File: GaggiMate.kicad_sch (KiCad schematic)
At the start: 48 parts, among them J1 BTNS, J15 HX711 connector, J2 Heater SSR, J3 K-Type probe, J4 Conn_02x08_Odd_Even, J5 Analog sensors, J6 Pressure Sensor, J7 Debug Pins, J8 HV In, J9 Relays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

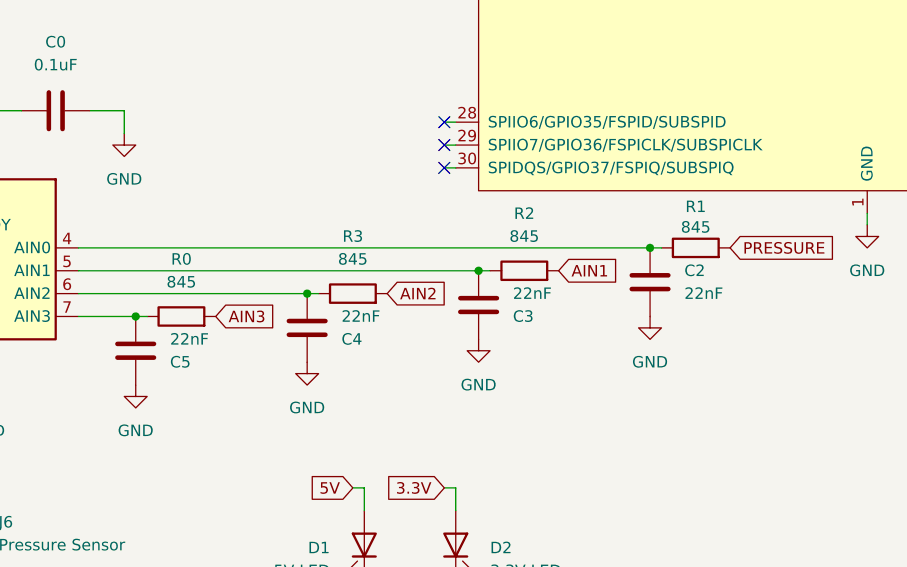
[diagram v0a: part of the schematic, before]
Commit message: update analog filters and started some HV traces
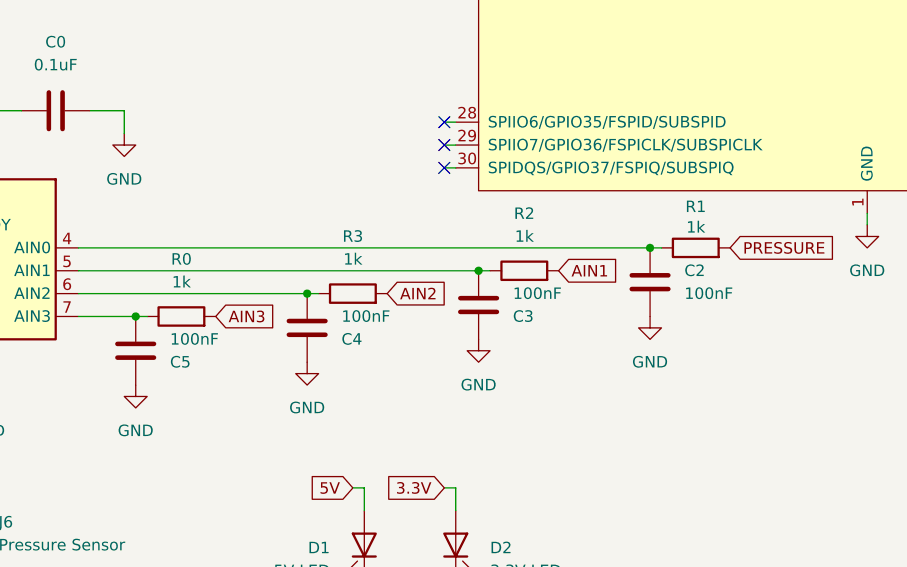
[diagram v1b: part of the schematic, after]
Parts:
- C2, C3, C4, C5: value 22nF -> 100nF
- R0, R1, R2, R3: value 845 -> 1k
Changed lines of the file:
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@@
 			)
 		)
-		(property "Value" "22nF"
+		(property "Value" "100nF"
 			(at 95.25 113.0301 0)
 			(effects
@@
 			)
 		)
-		(property "Value" "845"
+		(property "Value" "1k"
 			(at 77.47 109.22 90)
 			(effects
@@
 			)
 		)
-		(property "Value" "22nF"
+		(property "Value" "100nF"
 			(at 57.15 118.1101 0)
 			(effects
@@
 			)
 		)
-		(property "Value" "845"
+		(property "Value" "1k"
 			(at 115.57 105.664 90)
 			(effects
@@
 			)
 		)
-		(property "Value" "845"
+		(property "Value" "1k"
 			(at 96.52 106.68 90)
 			(effects
@@
 			)
 		)
-		(property "Value" "22nF"
+		(property "Value" "100nF"
 			(at 76.2 115.5701 0)
 			(effects
@@
 			)
 		)
-		(property "Value" "22nF"
+		(property "Value" "100nF"
 			(at 114.3 113.0299 0)
 			(effects
@@
 			)
 		)
-		(property "Value" "845"
+		(property "Value" "1k"
 			(at 58.42 111.76 90)
 			(effects

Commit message: more routing and and programming buttons
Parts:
- removed R4: 10k, Resistor_SMD:R_0603_1608Metric, symbol Device:R
- added C13, C14: 0.1uF, Capacitor_SMD:C_0603_1608Metric, symbol Device:C
- added C15: 10uF, Capacitor_SMD:C_0603_1608Metric, symbol Device:C
- added J16: UART, Connector_JST:JST_PH_B4B-PH-K_1x04_P2.00mm_Vertical, symbol Connector_Generic:Conn_01x04
- added SW1, SW2: SW_Push, Button_Switch_SMD:SW_SPST_TL3342, symbol Switch:SW_Push
- P0: footprint Connector_USB:USB_C_Receptacle_Palconn_UTC16-G -> Connector_USB:USB_C_Receptacle_HCTL_HC-TYPE-C-16P-01A
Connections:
- net 3.3V: now also R14.1; no longer R14.2
- net A0: no longer U2.37 (U0TXD/GPIO43/CLK_OUT1)
- net A1: no longer U2.36 (U0RXD/GPIO44/CLK_OUT2)
- net AIN1: now also J5.1 (Pin_1); no longer J5.3 (Pin_3)
- net AIN3: now also J5.3 (Pin_3); no longer J5.1 (Pin_1)
- net ALT: now also J7.6 (Pin_6); no longer J7.10 (Pin_10)
- net BOOT: now also C14.1, SW2.1; no longer R14.1
- net BREW_BTN: now also J7.10 (Pin_10); no longer J7.6 (Pin_6)
- net EN: now also R14.2, C13.1, C15.1, SW1.1
- net GND: now also C13.2, C14.2, C15.2, SW1.2, SW2.2
- net PUMP: now also J7.2 (Pin_2); no longer J7.4 (Pin_4)
- net VALVE: now also J7.4 (Pin_4); no longer J7.2 (Pin_2)
- net U0RTS: now reaches U2.8 (GPIO15/U0RTS/ADC2_CH4/XTAL_32K_P)
- net U0RTS: now also J16.1 (Pin_1)
- net U0CTS: now reaches U2.9 (GPIO16/U0CTS/ADC2_CH5/XTAL_32K_N)
- net U0CTS: now also J16.4 (Pin_4)
- net K-Probe T+ renamed T+
- net K-Probe T- renamed T-
- new net U0RXD: J16.3 (Pin_3), U2.36 (U0RXD/GPIO44/CLK_OUT2)
- new net U0TXD: J16.2 (Pin_2), U2.37 (U0TXD/GPIO43/CLK_OUT1)
- no-connect marks 6 -> 4
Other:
- moved on the sheet: C0, C1, C10, C11, C12, C2, C3, C4, C5, C6, C7, C8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

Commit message: finalize layout and tracks?
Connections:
- net D-: now reaches P0.A7 (D-), U4.1 (I/O1)
- net D+: now reaches P0.A6 (D+), U4.3 (I/O2)
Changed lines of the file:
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@@
+		)
+	)
+	(label "D-"
+		(at 63.5 48.26 0)
+		(effects
+			(font
+				(size 1.27 1.27)
+			)
+			(justify left bottom)
 		)
 	)
@@
 		(effects
 			(font
+				(size 1.27 1.27)
+			)
+			(justify left bottom)
+		)
+	)
+	(label "D+"
+		(at 63.5 53.34 0)
+		(effects
+			(font

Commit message: release candidate 1
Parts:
- removed C7: 10uF, Capacitor_SMD:C_0603_1608Metric, symbol Device:C
- removed D0: 1N5817, Diode_SMD:D_SOD-123, symbol Diode:1N5817
- removed J15: HX711 connector, symbol Connector_Generic:Conn_01x04
- removed J16: UART, Connector_JST:JST_PH_B4B-PH-K_1x04_P2.00mm_Vertical, symbol Connector_Generic:Conn_01x04
- removed J4: Conn_02x08_Odd_Even, Connector_PinHeader_2.54mm:PinHeader_2x08_P2.54mm_Vertical_SMD, symbol Connector_Generic:Conn_02x08_Odd_Even
- removed J7: Debug Pins, Connector_PinHeader_2.54mm:PinHeader_2x05_P2.54mm_Vertical_SMD, symbol Connector_Generic:Conn_02x05_Odd_Even
- removed P0: USB_C_Plug_USB2.0, Connector_USB:USB_C_Receptacle_HCTL_HC-TYPE-C-16P-01A, symbol Connector:USB_C_Plug_USB2.0
- removed R5, R6: 5.1k, Resistor_SMD:R_0603_1608Metric, symbol Device:R
- removed U4: USBLC6-2SC6, Package_TO_SOT_SMD:SOT-23-6, symbol Power_Protection:USBLC6-2SC6
- added C16: 10uF, Capacitor_SMD:C_0603_1608Metric, symbol Device:C
- added D3: 1N5817, Diode_SMD:D_SOD-123, symbol Diode:1N5817
- added J10: UART, Connector_PinHeader_2.54mm:PinHeader_2x02_P2.54mm_Vertical_SMD, symbol Connector_Generic:Conn_02x02_Odd_Even
- added J11: Fun breakout, Connector_PinHeader_2.54mm:PinHeader_2x03_P2.54mm_Vertical_SMD, symbol Connector_Generic:Conn_02x03_Odd_Even
- added J4: HX771, Connector_PinHeader_2.54mm:PinHeader_2x02_P2.54mm_Vertical_SMD, symbol Connector_Generic:Conn_02x02_Odd_Even
- added R17, R4: 5.1k, Resistor_SMD:R_0603_1608Metric, symbol Device:R
- added TP1, TP10, TP2, TP3, TP4, TP5, TP6, TP7, TP8, TP9: TestPoint, TestPoint:TestPoint_Pad_D1.0mm, symbol Connector:TestPoint
- added U7: GT-USB-7010ASV, easyeda2kicad:USB-C-SMD_G-SWITCH_GT-USB-7010ASV, symbol easyeda2kicad:GT-USB-7010ASV
- added U8: USBLC6-2SC6, Package_TO_SOT_SMD:SOT-23-6, symbol Power_Protection:USBLC6-2SC6
- J1, J2, J3, J5, J6, J8, J9, PS1: now fitted
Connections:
- net 3.3V: now also J4.4 (Pin_4), TP2.1; no longer D2.2 (A)
- net 5V: now also D3.1 (K), TP1.1
- net D+: now also U7.A6 (DP1), U7.B6 (DP2), U8.3 (I/O2)
- net D-: now also U7.A7 (DN1), U7.B7 (DN2), U8.1 (I/O1)
- net EN: now also D2.2 (A)
- net GND: now also C16.2, J11.2 (Pin_2), J4.2 (Pin_2), R17.2, R4.2, U7.1 (SHELL), U7.2 (SHELL), U7.3 (SHELL), U7.4 (SHELL), U7.A1B12 (GND), U7.B1A12 (GND), U8.2 (GND)
- net I2C_SCL: now also J4.3 (Pin_3), TP5.1
- net I2C_SDA: now also J4.1 (Pin_1), TP4.1
- net MAX_SPI_CS: now also TP9.1
- net SPI_CLK: now also TP8.1
- net SPI_MISO: now also TP6.1
- net SPI_MOSI: now also TP7.1
- net U0CTS: now also J10.1 (Pin_1)
- net U0RTS: now also J10.3 (Pin_3)
- net U0RXD: now also J10.2 (Pin_2)
- net U0TXD: now also J10.4 (Pin_4)
- net USB_D+: now also U8.4 (I/O2)
- net USB_D-: now also U8.6 (I/O1)
- net A10 renamed IO6
- net IO6: now also J11.6 (Pin_6)
- net A11: no longer names the net of U2.23 (GPIO21)
- net A12: no longer names the net of U2.26 (GPIO45)
- net A13: no longer names the net of U2.16 (GPIO46)
- net A13: now also TP10.1
- net A2: no longer names the net of U2.39 (GPIO1/TOUCH1/ADC1_CH0)
- net A3: no longer names the net of U2.38 (GPIO2/TOUCH2/ADC1_CH1)
- net A4: no longer names the net of U2.15 (GPIO3/TOUCH3/ADC1_CH2)
- net A4: now also TP3.1
- net A5 renamed IO1
- net IO1: now also J11.1 (Pin_1)
- net A6 renamed IO2
- net IO2: now also J11.3 (Pin_3)
- net A7 renamed IO3
- net IO3: now also J11.5 (Pin_5)
- net A8: no longer names the net of U2.21 (GPIO13/TOUCH13/ADC2_CH2/FSPIQ/FSPIIO7/SUBSPIQ)
- net A9 renamed IO5
- net IO5: now also J11.4 (Pin_4)
- new net: C16.1, D3.2 (A), U7.A4B9 (VBUS), U7.B4A9 (VBUS), U8.5 (VBUS)
- new net: R17.1, U7.A5 (CC1)
- new net: R4.1, U7.B5 (CC2)
- no-connect marks 4 -> 6
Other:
- removed sheet Extra components

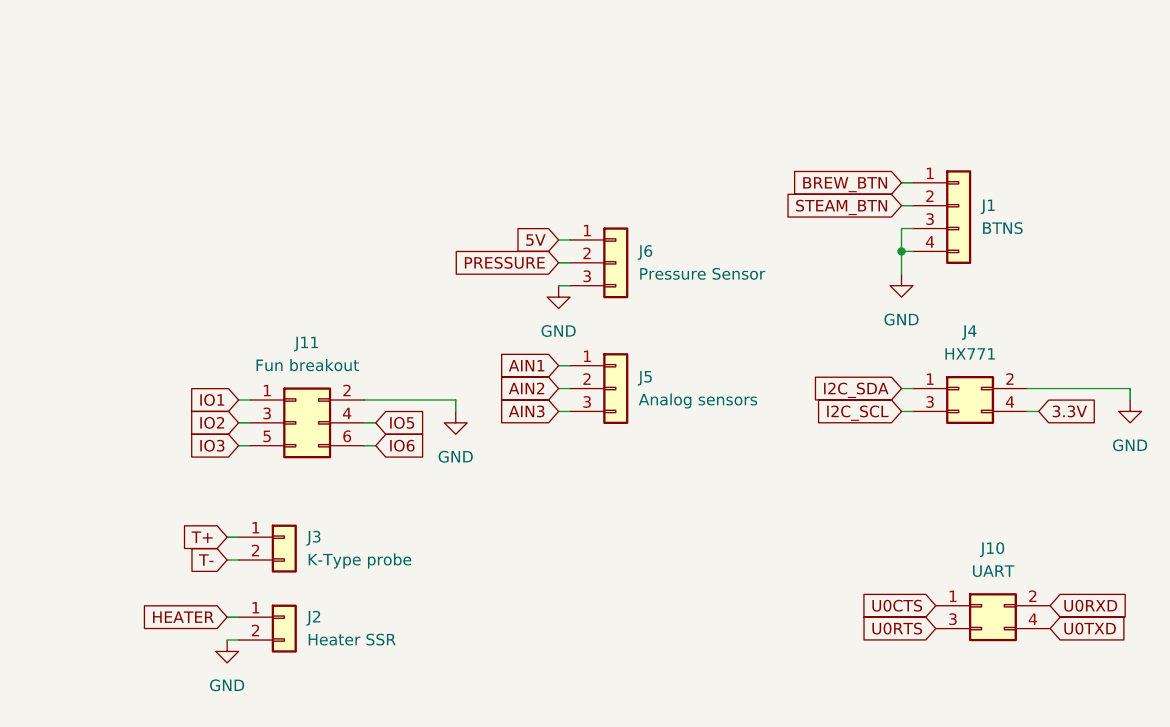
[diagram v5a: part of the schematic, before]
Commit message: add custom silkscreen and missing lilygo out pins
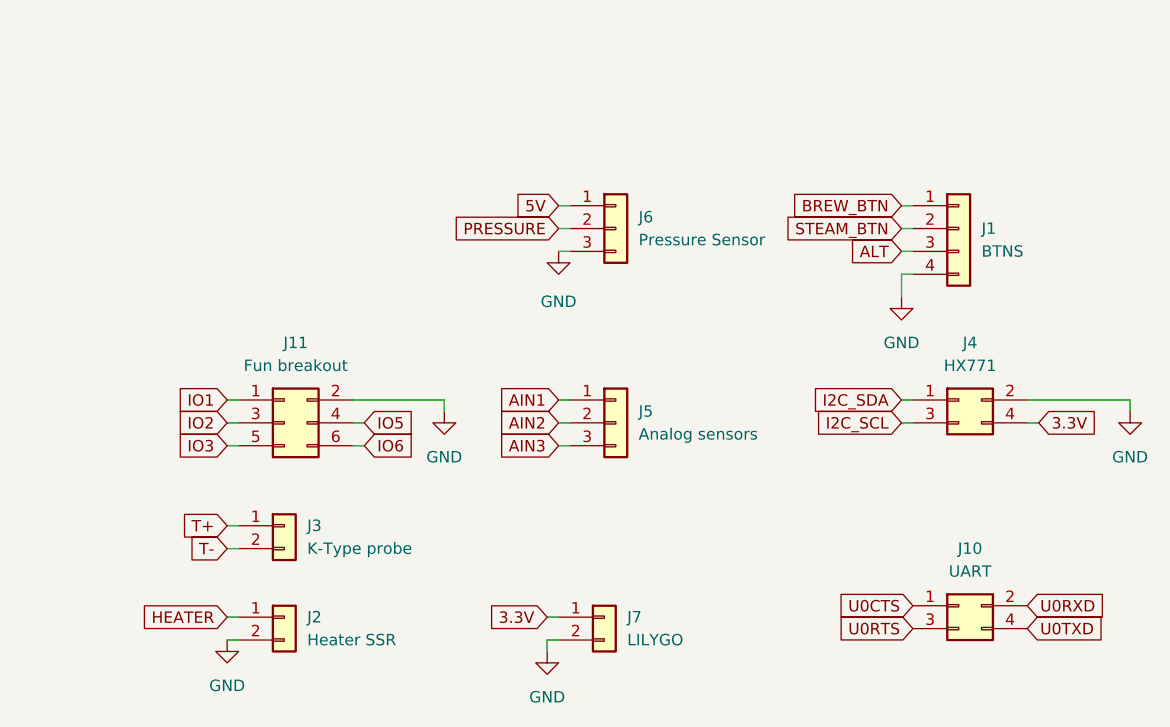
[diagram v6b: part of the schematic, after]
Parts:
- added J7: LILYGO, Connector_JST:JST_PH_B2B-PH-K_1x02_P2.00mm_Vertical, symbol Connector_Generic:Conn_01x02
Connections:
- net 3.3V: now also J7.1 (Pin_1)
- net ALT: now also J1.3 (Pin_3)
- net GND: now also J7.2 (Pin_2); no longer J1.3 (Pin_3)
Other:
- moved on the sheet: J1, J10, J11, J3, J4, J5, J6

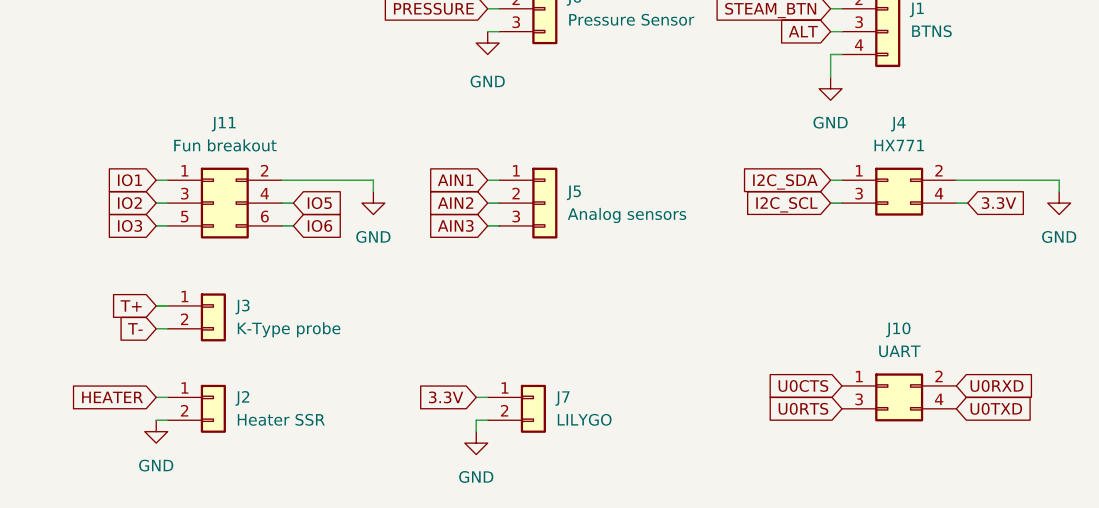
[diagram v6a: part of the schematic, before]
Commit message: update to new footprint ad make stuff nice
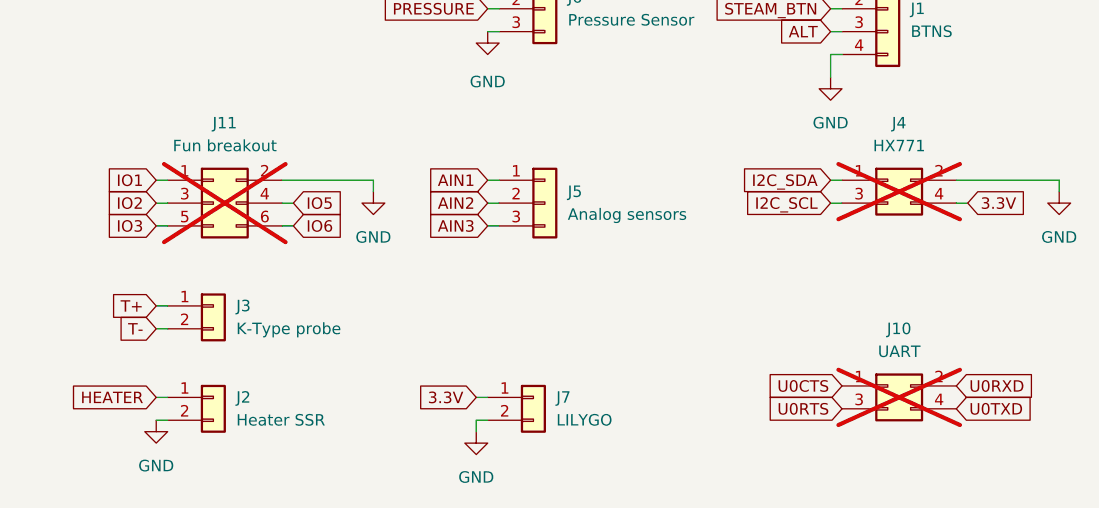
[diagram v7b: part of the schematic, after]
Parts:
- J10, J11, J4: now not fitted
- U2: footprint PCM_Espressif:ESP32-S3-WROOM-1 -> easyeda2kicad:WIRELM-SMD_ESP32-S3-WROOM-1
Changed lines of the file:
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@@
 		(in_bom yes)
 		(on_board yes)
-		(dnp no)
+		(dnp yes)
 		(fields_autoplaced yes)
 		(property "Reference" "J4"
@@
 			)
 		)
-		(property "Footprint" "PCM_Espressif:ESP32-S3-WROOM-1"
+		(property "Footprint" "easyeda2kicad:WIRELM-SMD_ESP32-S3-WROOM-1"
 			(at 222.25 119.38 0)
 			(effects
@@
 		(in_bom yes)
 		(on_board yes)
-		(dnp no)
+		(dnp yes)
 		(fields_autoplaced yes)
 		(property "Reference" "J10"
@@
 		(in_bom yes)
 		(on_board yes)
-		(dnp no)
+		(dnp yes)
 		(fields_autoplaced yes)
 		(property "Reference" "J11"

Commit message: add missing models and finalize pcb
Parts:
- added D4, D5: 3.3V LED, LED_SMD:LED_0603_1608Metric, symbol Device:LED
- added R6, R7: 150, Resistor_SMD:R_0603_1608Metric, symbol Device:R
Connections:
- net GND: now also R6.2, R7.2
- net LED2: now reaches U2.38 (GPIO2/TOUCH2/ADC1_CH1)
- net LED2: now also D5.2 (A)
- net LED1: now reaches U2.39 (GPIO1/TOUCH1/ADC1_CH0)
- net LED1: now also D4.2 (A)
- new net: D5.1 (K), R7.1
- new net: D4.1 (K), R6.1
- no-connect marks 6 -> 9
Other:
- moved on the sheet: D1, D2, R13, TP6, TP7, TP8
